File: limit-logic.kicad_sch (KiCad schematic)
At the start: 4 parts, among them U17001 CD4044, U17002 CD4044

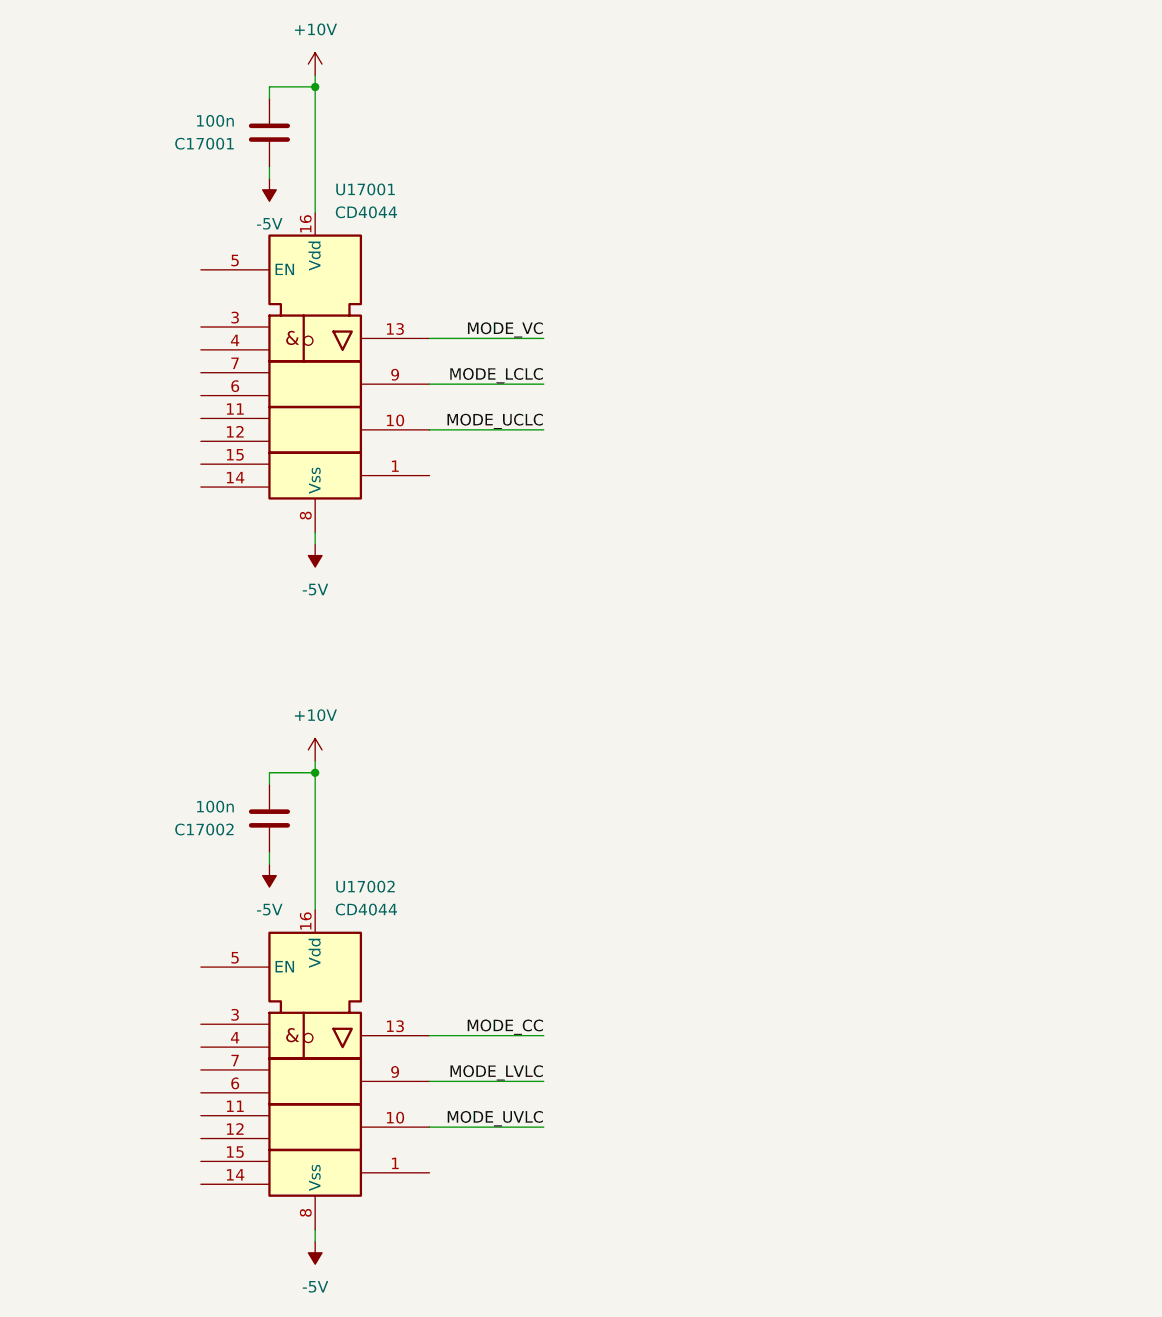
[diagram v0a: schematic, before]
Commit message: move symbols to project specific library
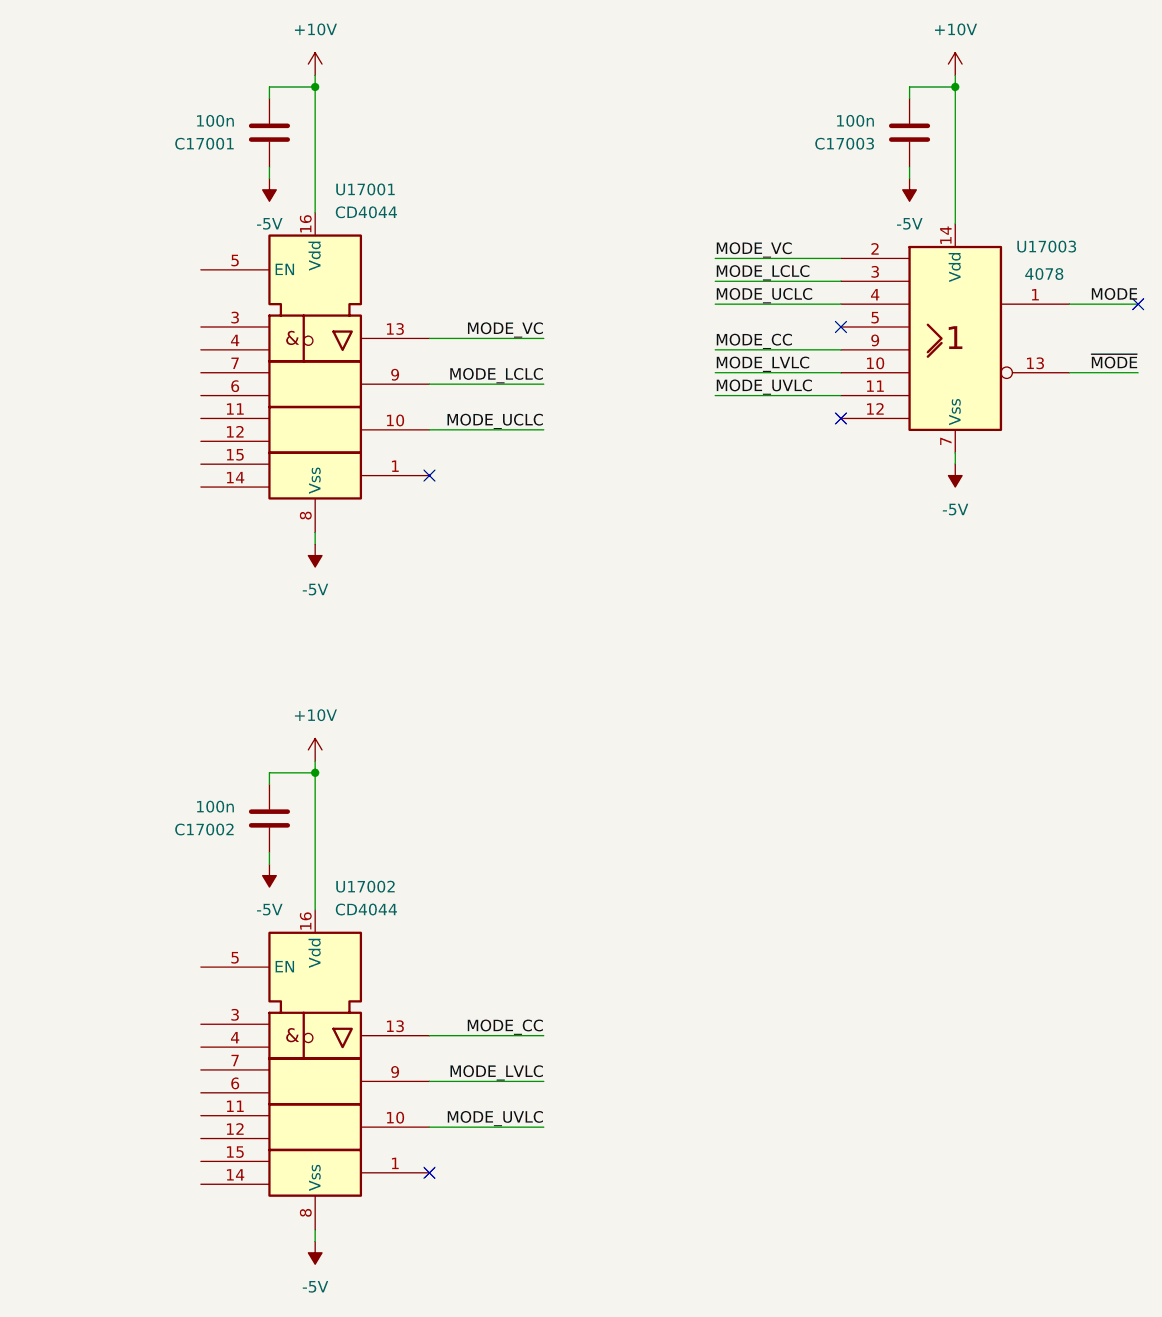
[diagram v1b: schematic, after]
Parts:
- added C17003: 100n, Capacitor_SMD:C_0805_2012Metric_Pad1.18x1.45mm_HandSolder, symbol pss:C
- added U17003: 4078, symbol pss:4078
- C17001, C17002: symbol Device:C -> pss:C
- U17001, U17002: symbol 4xxx_IEEE:4044 -> pss:4044
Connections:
- net +10V: now also C17003.2, U17003.14 (Vdd)
- net -5V: now also C17003.1, U17003.7 (Vss)
- net MODE_CC: now also U17003.9
- net MODE_LCLC: now also U17003.3
- net MODE_LVLC: now also U17003.10
- net MODE_UCLC: now also U17003.4
- net MODE_UVLC: now also U17003.11
- net MODE_VC: now also U17003.2
- new net MODE: U17003.1
- new net ~{MODE}: U17003.13
- no-connect marks 0 -> 5

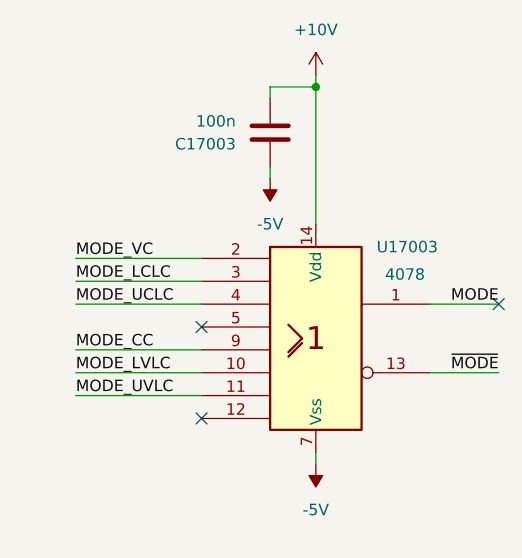
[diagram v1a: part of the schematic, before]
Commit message: add limit-logic mode NOR gate 4078
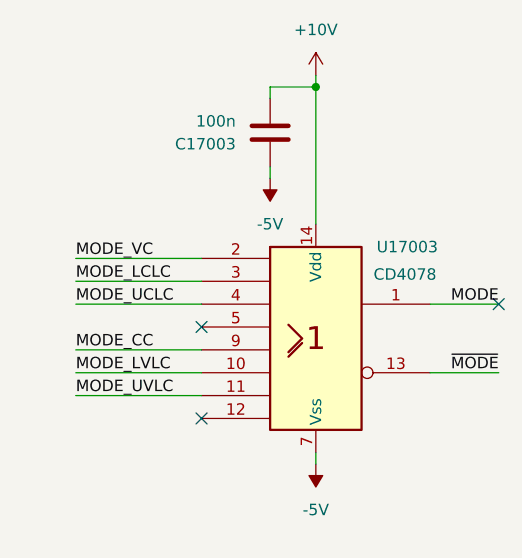
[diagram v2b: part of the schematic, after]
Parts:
- U17003: value 4078 -> CD4078; footprint (none) -> Package_SO:SOIC-14_3.9x8.7mm_P1.27mm; MPN (none) -> CD4078BM96; VPN (none) -> 595-CD4078BM96
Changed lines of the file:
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@@
 			)
 		)
-		(property "Value" "4078"
+		(property "Value" "CD4078"
 			(at 258.826 47.498 0)
 			(effects
@@
 			)
 		)
-		(property "Footprint" ""
+		(property "Footprint" "Package_SO:SOIC-14_3.9x8.7mm_P1.27mm"
 			(at 248.92 54.61 0)
 			(effects
@@
 			)
 		)
-		(property "Datasheet" ""
+		(property "Datasheet" "https://www.ti.com/lit/ds/symlink/cd4078b.pdf"
 			(at 248.92 54.61 0)
 			(effects
@@
 			(at 248.92 54.61 0)
 			(effects
+				(font
+					(size 1.27 1.27)
+				)
+				(hide yes)
+			)
+		)
+		(property "MPN" "CD4078BM96"
+			(at 248.92 54.61 0)
+			(effects
+				(font
+					(size 1.27 1.27)
+				)
+				(hide yes)
+			)
+		)
+		(property "VPN" "595-CD4078BM96"
+			(at 248.92 54.61 0)
+			(effects

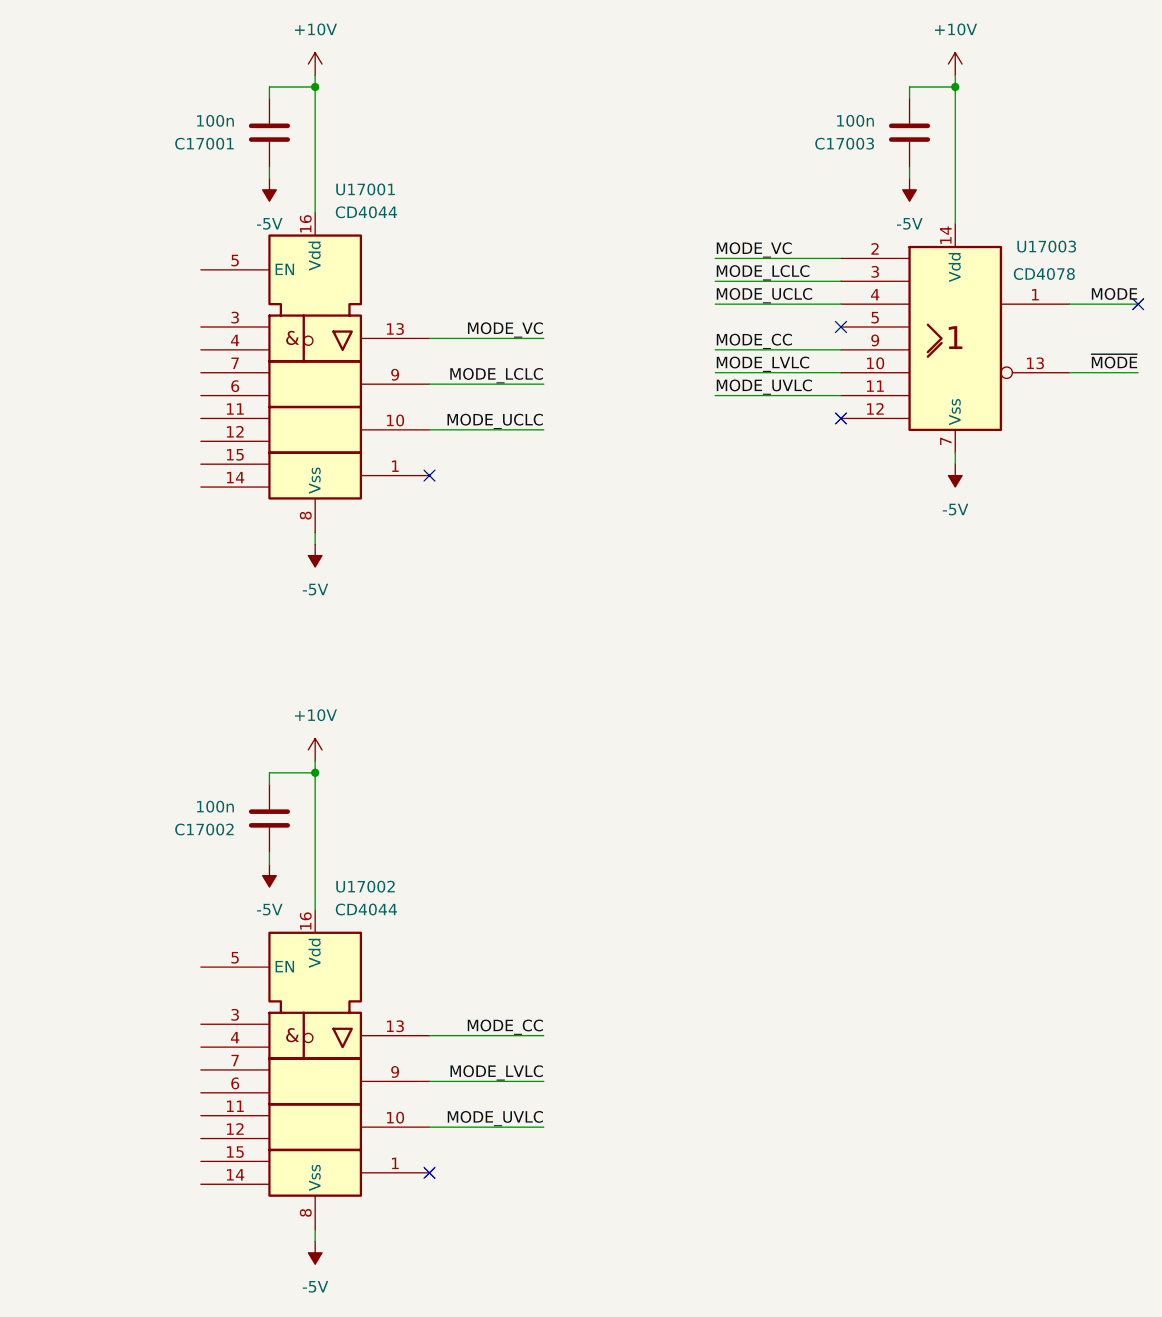
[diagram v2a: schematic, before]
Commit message: add limit-logic pull ups/downs for input pins
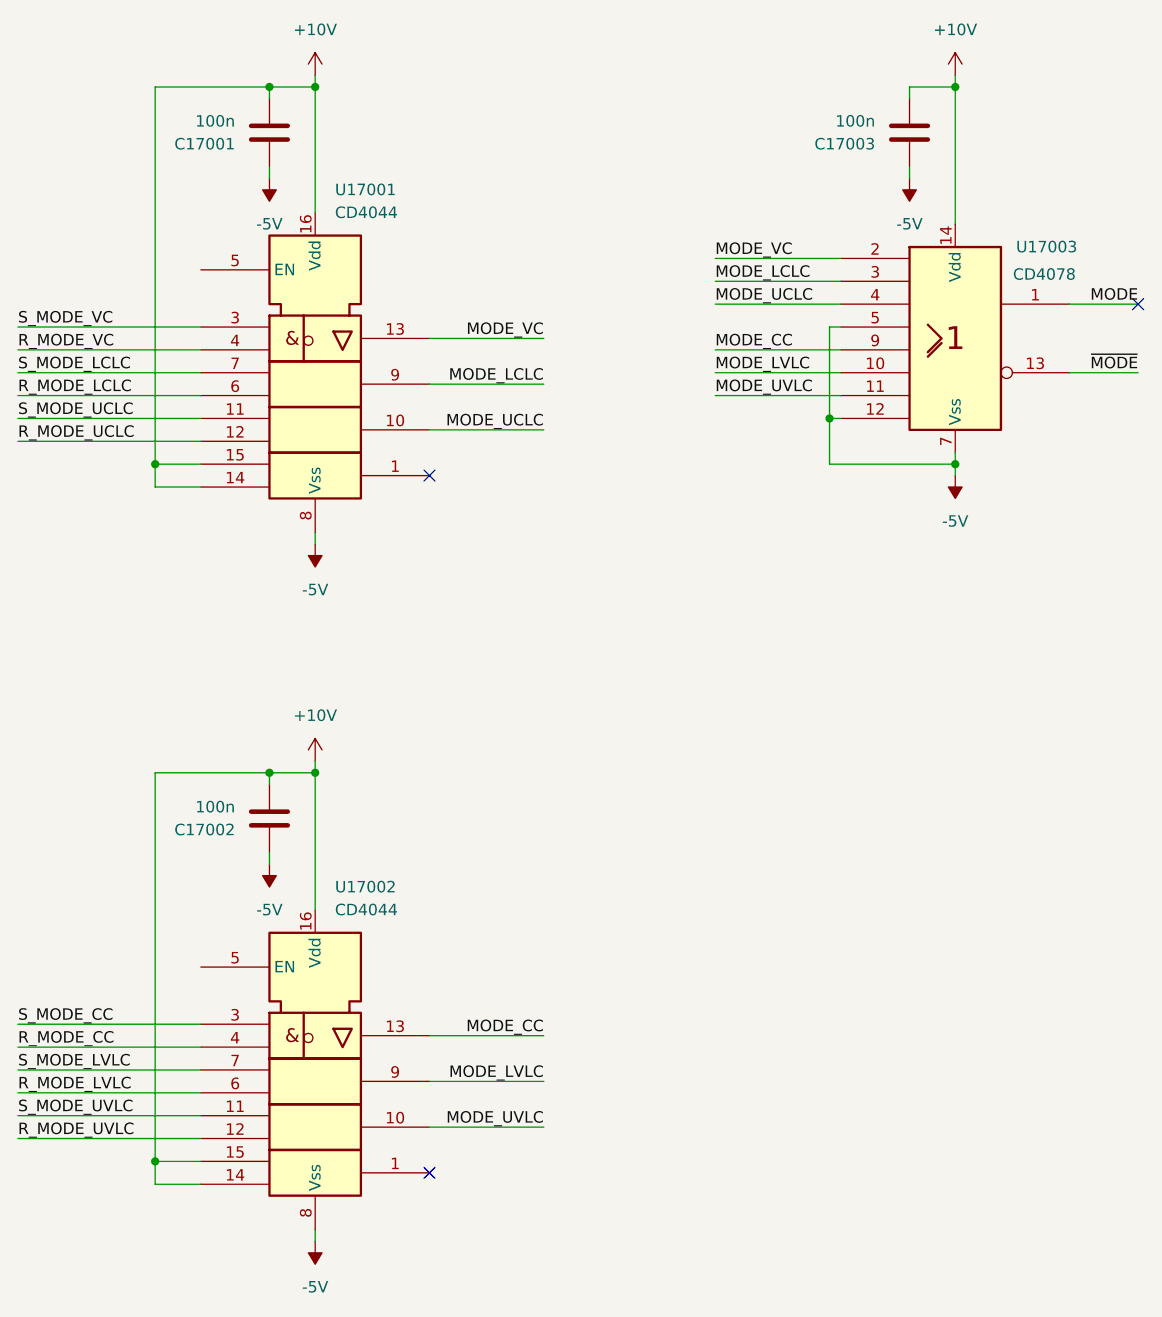
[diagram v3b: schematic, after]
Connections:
- net +10V: now also U17001.14, U17001.15, U17002.14, U17002.15
- net -5V: now also U17003.12, U17003.5
- net S_MODE_UVLC: now reaches U17002.11
- net R_MODE_UVLC: now reaches U17002.12
- net S_MODE_CC: now reaches U17002.3
- net R_MODE_CC: now reaches U17002.4
- net R_MODE_LVLC: now reaches U17002.6
- net S_MODE_LVLC: now reaches U17002.7
- net S_MODE_UCLC: now reaches U17001.11
- net R_MODE_UCLC: now reaches U17001.12
- net S_MODE_VC: now reaches U17001.3
- net R_MODE_VC: now reaches U17001.4
- net R_MODE_LCLC: now reaches U17001.6
- net S_MODE_LCLC: now reaches U17001.7
- no-connect marks 5 -> 3
